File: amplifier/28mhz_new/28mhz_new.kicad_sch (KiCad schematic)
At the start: 32 parts, among them M1 RD16HHF1, Q1 LG, Q2 L6, Q3 LG, Q4 LG, Q5 LG

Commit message: Assigned all footprints
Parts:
- added RE3: 330, Resistor_SMD:R_1206_3216Metric_Pad1.30x1.75mm_HandSolder, symbol ltspice:res
- C1, C10, C14, C2, C6, C8, C9: footprint (none) -> Capacitor_SMD:C_0805_2012Metric_Pad1.18x1.45mm_HandSolder
- L1: footprint (none) -> B82144A2103K:INDAD3280W80L1200D520
- L2: footprint (none) -> 2929SQ-331GEC:2929SQ331GEC
- L5: footprint (none) -> 2222SQ:2222SQ181JEC
- L6, L7: footprint (none) -> 2929SQ-391GEC:2929SQ391GEC
- L8: value 440n -> 430n; footprint (none) -> 2929SQ-431GEC:2929SQ431GEC
- M1: footprint (none) -> Package_TO_SOT_THT:TO-220-3_Vertical
- Q1, Q3, Q4, Q5: value LG -> 2N3904; footprint (none) -> Package_TO_SOT_THT:TO-92L_HandSolder
- Q2: value L6 -> 2N3906; footprint (none) -> Package_TO_SOT_THT:TO-92L_HandSolder
- R1, R18, R9: footprint (none) -> Resistor_SMD:R_1206_3216Metric_Pad1.30x1.75mm_HandSolder
- R10, R11, R12, R13, R17, R20, R4, R8: footprint (none) -> Resistor_SMD:R_0603_1608Metric_Pad0.98x0.95mm_HandSolder
- R3: value 3.4k -> 3.3k; footprint (none) -> Resistor_SMD:R_0603_1608Metric_Pad0.98x0.95mm_HandSolder
- R7: value 165 -> 330; footprint (none) -> Resistor_SMD:R_1206_3216Metric_Pad1.30x1.75mm_HandSolder
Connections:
- net 0: now also M1.2 (S), RE3.2; no longer M1.3 (S)
- net VCC: now also R18.1
- net at C1.1, C2.2, L1.2: now also M1.3 (D); no longer M1.1 (D)
- net at Q2.3 (E), Q3.3 (E): now also M1.1 (G); no longer M1.2 (G)
- net at Q1.3 (E), R12.2, R13.1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: now also RE3.1
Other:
- note added: "IDEA: make this an RPi hat! If a user doesn't want to use it as a hat, then just solder directly to pins"
- moved on the sheet: R18, R7

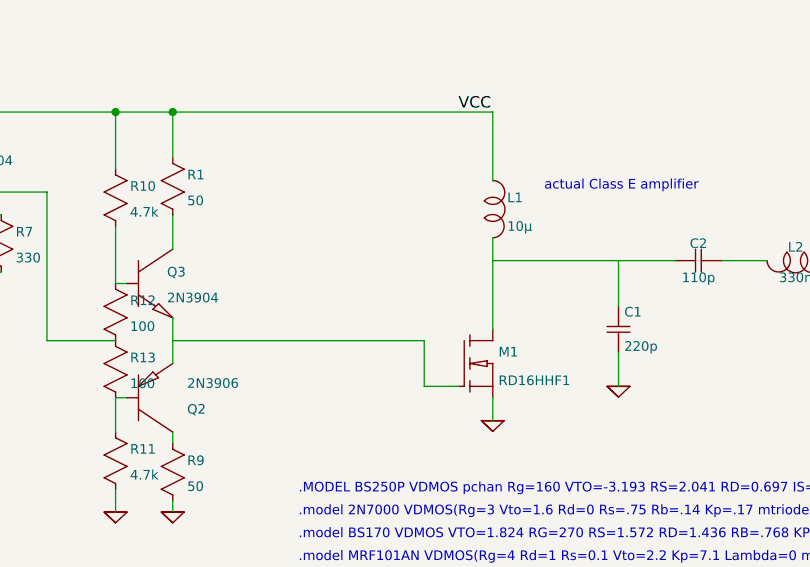
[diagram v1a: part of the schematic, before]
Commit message: This looks nice, but I'm realizing soldering it will be basically impossible
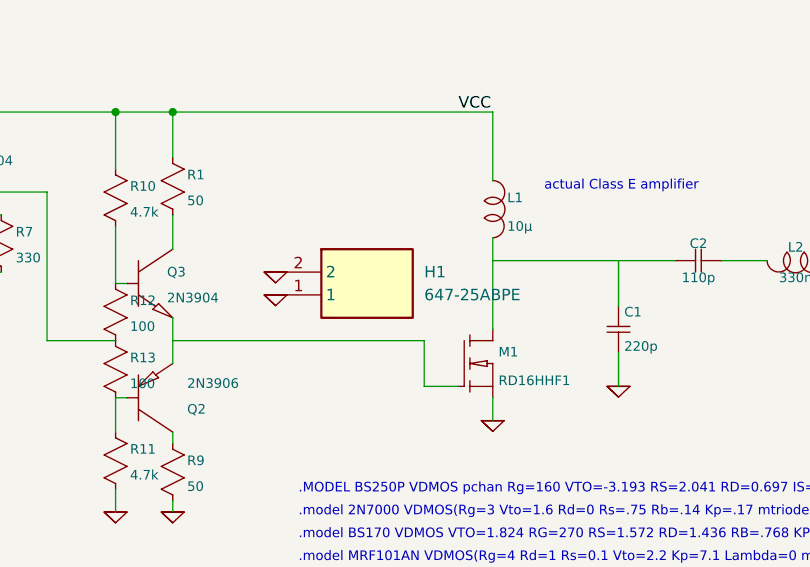
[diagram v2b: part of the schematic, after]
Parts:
- added H1: 647-25ABPE, 64725ABPE, symbol heatsink:647-25ABPE
- Q1, Q2, Q3, Q4, Q5: footprint Package_TO_SOT_THT:TO-92L_HandSolder -> Package_TO_SOT_THT:TO-92L_Inline
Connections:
- net 0: now also H1.1, H1.2

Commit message: NO DRC ERRORS
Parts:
- R10, R11, R12, R13, R20, R3, R4, R8: footprint Resistor_SMD:R_0603_1608Metric_Pad0.98x0.95mm_HandSolder -> Resistor_SMD:R_0805_2012Metric_Pad1.20x1.40mm_HandSolder
- R17: footprint Resistor_SMD:R_0603_1608Metric_Pad0.98x0.95mm_HandSolder -> Resistor_SMD:R_1206_3216Metric_Pad1.30x1.75mm_HandSolder
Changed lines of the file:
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@@
 			)
 		)
-		(property "Footprint" "Resistor_SMD:R_0603_1608Metric_Pad0.98x0.95mm_HandSolder"
+		(property "Footprint" "Resistor_SMD:R_0805_2012Metric_Pad1.20x1.40mm_HandSolder"
 			(at 86.36 102.87 0)
 			(effects
@@
 			)
 		)
-		(property "Description" "RT0603FRE071KL "
+		(property "Description" "RT0805FRE071KL "
 			(at 86.36 102.87 0)
 			(effects
@@
 			)
 		)
-		(property "Footprint" "Resistor_SMD:R_0603_1608Metric_Pad0.98x0.95mm_HandSolder"
+		(property "Footprint" "Resistor_SMD:R_0805_2012Metric_Pad1.20x1.40mm_HandSolder"
 			(at 93.98 107.95 0)
 			(effects
@@
 			)
 		)
-		(property "Description" "RT0603FRE0733RL"
+		(property "Description" "RT0805FRE0733RL"
 			(at 93.98 107.95 0)
 			(effects
@@
 			)
 		)
-		(property "Footprint" "Resistor_SMD:R_0603_1608Metric_Pad0.98x0.95mm_HandSolder"
+		(property "Footprint" "Resistor_SMD:R_0805_2012Metric_Pad1.20x1.40mm_HandSolder"
 			(at 121.92 82.55 0)
 			(effects
@@
 			)
 		)
-		(property "Description" "RT0603FRE074K7L"
+		(property "Description" "RT0805FRE074K7L"
 			(at 121.92 82.55 0)
 			(effects
@@
 			)
 		)
-		(property "Footprint" "Resistor_SMD:R_0603_1608Metric_Pad0.98x0.95mm_HandSolder"
+		(property "Footprint" "Resistor_SMD:R_0805_2012Metric_Pad1.20x1.40mm_HandSolder"
 			(at 121.92 101.6 0)
 			(effects
@@
 			)
 		)
-		(property "Description" "RT0603FRE07100RL"
+		(property "Description" "RT0805FRE07100RL"
 			(at 121.92 101.6 0)
 			(effects
@@
 			)
 		)
-		(property "Footprint" "Resistor_SMD:R_0603_1608Metric_Pad0.98x0.95mm_HandSolder"
+		(property "Footprint" "Resistor_SMD:R_1206_3216Metric_Pad1.30x1.75mm_HandSolder"
 			(at 68.58 102.87 0)
 			(effects
@@
 			)
 		)
-		(property "Description" "RT0603DRD07330RL"
+		(property "Description" "TNPW1206330RBEEA"
 			(at 68.58 102.87 0)
 			(effects
@@
 			)
 		)
-		(property "Footprint" "Resistor_SMD:R_0603_1608Metric_Pad0.98x0.95mm_HandSolder"
+		(property "Footprint" "Resistor_SMD:R_0805_2012Metric_Pad1.20x1.40mm_HandSolder"
 			(at 87.63 83.82 0)
 			(effects
@@
 			)
 		)
-		(property "Description" "RT0603FRE0710KL "
+		(property "Description" "RT0805FRE0710KL "
 			(at 87.63 83.82 0)
 			(effects
@@
 			)
 		)
-		(property "Footprint" "Resistor_SMD:R_0603_1608Metric_Pad0.98x0.95mm_HandSolder"
+		(property "Footprint" "Resistor_SMD:R_0805_2012Metric_Pad1.20x1.40mm_HandSolder"
 			(at 87.63 90.17 0)
 			(effects
@@
 			)
 		)
-		(property "Description" "RT0603FRD073K3L "
+		(property "Description" "RT0805FRD073K3L "
 			(at 87.63 90.17 0)
 			(effects
@@
 			)
 		)
-		(property "Footprint" "Resistor_SMD:R_0603_1608Metric_Pad0.98x0.95mm_HandSolder"
+		(property "Footprint" "Resistor_SMD:R_0805_2012Metric_Pad1.20x1.40mm_HandSolder"
 			(at 121.92 111.76 0)
 			(effects
@@
 			)
 		)
-		(property "Description" "RT0603FRE074K7L"
+		(property "Description" "RT0805FRE074K7L"
 			(at 121.92 111.76 0)
 			(effects
@@
 			)
 		)
-		(property "Footprint" "Resistor_SMD:R_0603_1608Metric_Pad0.98x0.95mm_HandSolder"
+		(property "Footprint" "Resistor_SMD:R_0805_2012Metric_Pad1.20x1.40mm_HandSolder"
 			(at 121.92 95.25 0)
 			(effects
@@
 			)
 		)
-		(property "Description" "RT0603FRE07100RL"
+		(property "Description" "RT0805FRE07100RL"
 			(at 121.92 95.25 0)
 			(effects

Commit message: SEND IT (in the morning once i have sanity checked)
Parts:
- added B1: CONBNC002, BNC:CONBNC002, symbol BNC:CONBNC002
- added J1: GPIO, Connector_PinSocket_2.54mm:PinSocket_2x20_P2.54mm_Vertical, symbol Connector_Generic:Conn_02x20_Odd_Even
- added J2: 694106301002, barreljack:694106301002_1, symbol barreljack:694106301002
- H1: footprint 64725ABPE -> heatsink:64725ABPE
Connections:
- net 0: now also B1.1, J1.14 (Pin_14), J1.20 (Pin_20), J1.25 (Pin_25), J1.30 (Pin_30), J1.34 (Pin_34), J1.39 (Pin_39), J1.6 (Pin_6), J1.9 (Pin_9), J2.2 (GND_1), J2.3 (GND_2)
- net RF_OUT: now also B1.2
- net VCC: now also J2.1 (POWER)
- net RF_IN renamed GPIO4/GPCLK0
- new net +3V3: J1.1 (Pin_1), J1.17 (Pin_17)
- new net +5V: J1.2 (Pin_2), J1.4 (Pin_4)
- new net GPIO10/SPI0.MOSI: J1.19 (Pin_19)
- new net GPIO11/SPI0.SCLK: J1.23 (Pin_23)
- new net GPIO12/PWM0: J1.32 (Pin_32)
- new net GPIO13/PWM1: J1.33 (Pin_33)
- new net GPIO14/TXD0: J1.8 (Pin_8)
- new net GPIO15/RXD0: J1.10 (Pin_10)
- new net GPIO16: J1.36 (Pin_36)
- new net GPIO17: J1.11 (Pin_11)
- new net GPIO18/PCM.CLK: J1.12 (Pin_12)
- new net GPIO19/PCM.FS: J1.35 (Pin_35)
- new net GPIO20/PCM.DIN: J1.38 (Pin_38)
- new net GPIO21/PCM.DOUT: J1.40 (Pin_40)
- new net GPIO22: J1.15 (Pin_15)
- new net GPIO23: J1.16 (Pin_16)
- new net GPIO24: J1.18 (Pin_18)
- new net GPIO25: J1.22 (Pin_22)
- new net GPIO26: J1.37 (Pin_37)
- new net GPIO27: J1.13 (Pin_13)
- new net GPIO2/SDA1: J1.3 (Pin_3)
- new net GPIO3/SCL1: J1.5 (Pin_5)
- new net GPIO4/GPCLK0: J1.7 (Pin_7)
- new net GPIO5: J1.29 (Pin_29)
- new net GPIO6: J1.31 (Pin_31)
- new net GPIO7/SPI0.CE1: J1.26 (Pin_26)
- new net GPIO8/SPI0.CE0: J1.24 (Pin_24)
- new net GPIO9/SPI0.MISO: J1.21 (Pin_21)
- new net ID_SCL: J1.28 (Pin_28)
- new net ID_SDA: J1.27 (Pin_27)
- no-connect marks 0 -> 2
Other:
- moved on the sheet: C1, C10, C14, C2, C6, C8, C9, H1, L1, L2, L5, L6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

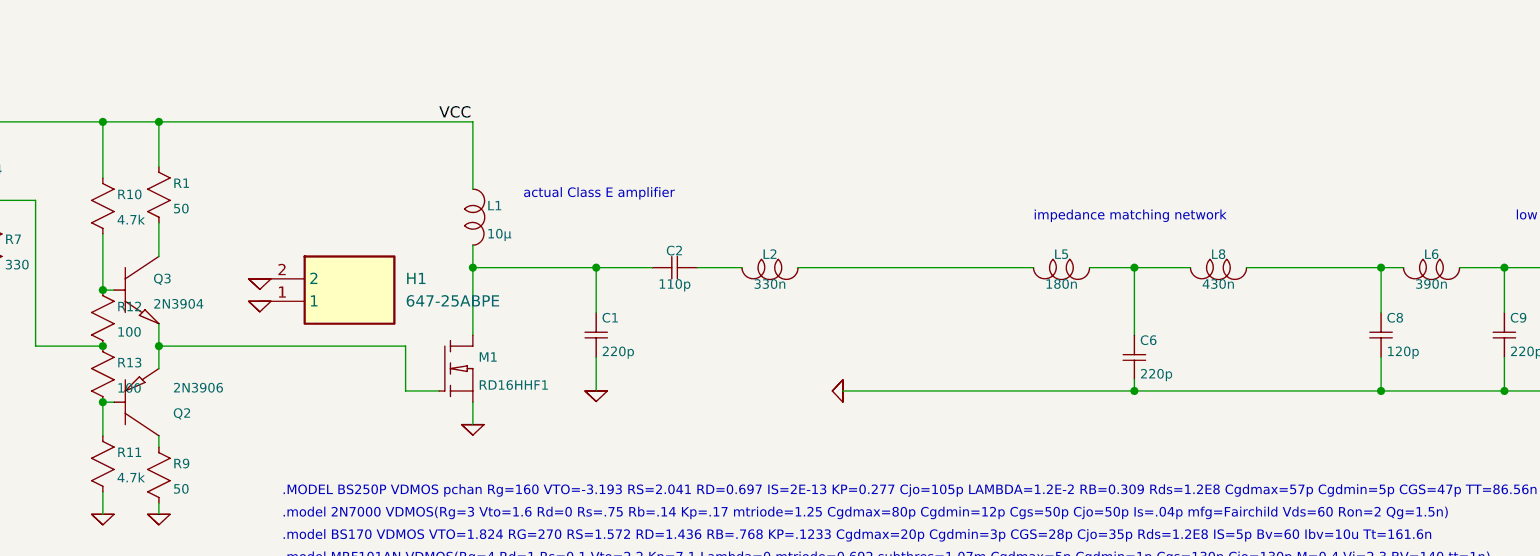
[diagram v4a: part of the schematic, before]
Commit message: Add zero ohm resistors
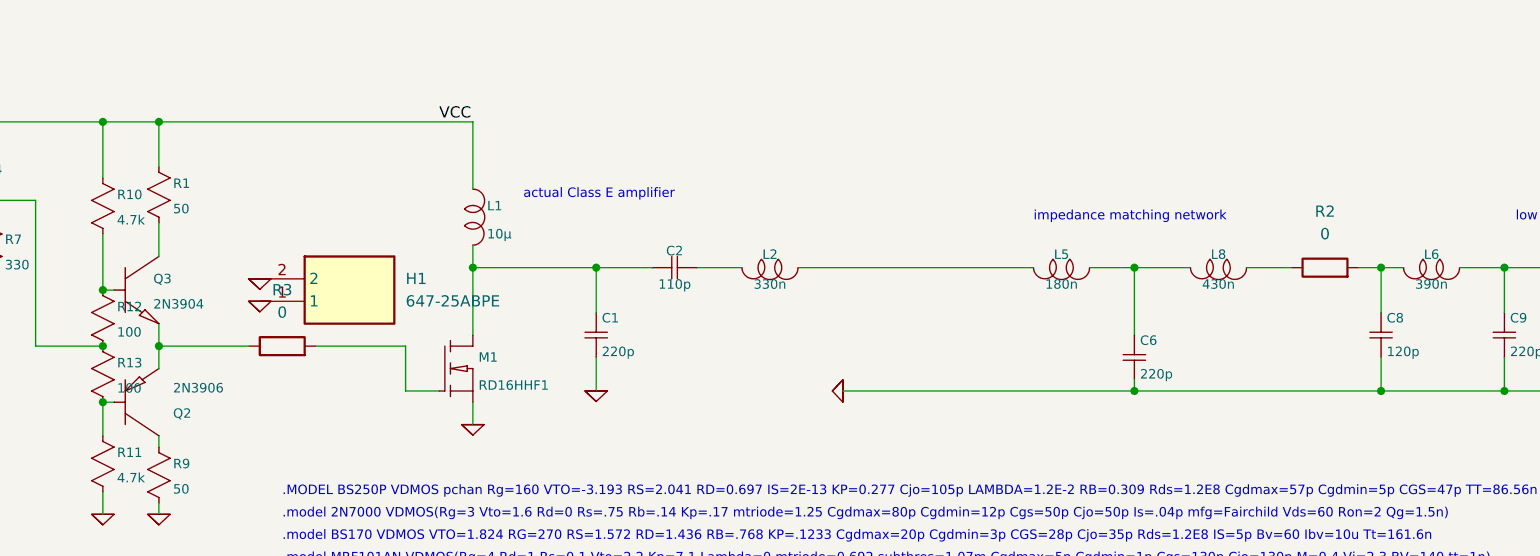
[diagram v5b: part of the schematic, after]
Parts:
- added R2, R3: 0, Resistor_SMD:R_2512_6332Metric, symbol Device:R
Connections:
- net at Q2.3 (E), Q3.3 (E): now also R3.1; no longer M1.1 (G)
- net at C8.1, L6.2: now also R2.2; no longer L8.1
- new net: L8.1, R2.1
- new net: M1.1 (G), R3.2
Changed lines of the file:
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@@
 	(wire
 		(pts
+			(xy 222.25 93.98) (xy 217.17 93.98)
+		)
+		(stroke
+			(width 0.1524)
+			(type solid)
+		)
+	)
+	(wire
+		(pts
 			(xy 262.89 93.98) (xy 269.24 93.98)
 		)
@@
 	(wire
 		(pts
-			(xy 232.41 93.98) (xy 217.17 93.98)
+			(xy 104.14 102.87) (xy 93.98 102.87)
+		)
+		(stroke
+			(width 0.1524)
+			(type solid)
+		)
+	)
+	(wire
+		(pts
+			(xy 232.41 93.98) (xy 229.87 93.98)
 		)
 		(stroke
@@
 	(wire
 		(pts
-			(xy 121.92 102.87) (xy 93.98 102.87)
+			(xy 121.92 102.87) (xy 111.76 102.87)
 		)
 		(stroke
@@
 	)
 	(symbol
+		(lib_id "Device:R")
+		(at 107.95 102.87 90)
+		(unit 1)
+		(exclude_from_sim no)
+		(in_bom yes)
+		(on_board yes)
+		(dnp no)
+		(fields_autoplaced yes)
+		(property "Reference" "R3"
+			(at 107.95 96.52 90)
+			(effects
+				(font
+					(size 1.27 1.27)
+				)
+			)
+		)
+		(property "Value" "0"
+			(at 107.95 99.06 90)
+			(effects
+				(font
+					(size 1.27 1.27)
+				)
+			)
+		)
+		(property "Footprint" "Resistor_SMD:R_2512_6332Metric"
+			(at 107.95 104.648 90)
+			(effects
+				(font
+					(size 1.27 1.27)
+				)
+				(hide yes)
+			)
+		)
+		(property "Datasheet" "~"
+			(at 107.95 102.87 0)
+			(effects
+				(font
+					(size 1.27 1.27)
+				)
+				(hide yes)
+			)
+		)
+		(property "Description" "Resistor"
+			(at 107.95 102.87 0)
+			(effects
+				(font
+					(size 1.27 1.27)
+				)
+				(hide yes)
+			)
+		)
+		(pin "2"
+		)
+		(pin "1"
+		)
+		(instances
+			(project "28mhz_new"
+				(path "/a27f0a38-2c6c-4fbf-aebb-5f1ef9203ab8"
+					(reference "R3")
+					(unit 1)
+				)
+			)
+		)
+	)
+	(symbol
 		(lib_id "ltspice:res")
 		(at 86.36 101.6 0)
@@
 					(unit 1)
 				)
+			)
+		)
+	)
+	(symbol
+		(lib_id "Device:R")
+		(at 226.06 93.98 90)
+		(unit 1)
+		(exclude_from_sim no)
+		(in_bom yes)
+		(on_board yes)
+		(dnp no)
+		(fields_autoplaced yes)
+		(property "Reference" "R2"
+			(at 226.06 87.63 90)
+			(effects
+				(font
+					(size 1.27 1.27)
+				)
+			)
+		)
+		(property "Value" "0"
+			(at 226.06 90.17 90)
+			(effects
+				(font
+					(size 1.27 1.27)
+				)
+			)
+		)
+		(property "Footprint" "Resistor_SMD:R_2512_6332Metric"
+			(at 226.06 95.758 90)
+			(effects
+				(font
+					(size 1.27 1.27)
+				)
+				(hide yes)
+			)
+		)
+		(property "Datasheet" "~"
+			(at 226.06 93.98 0)
+			(effects
+				(font
+					(size 1.27 1.27)
+				)
+				(hide yes)
+			)
+		)
+		(property "Description" "Resistor"
+			(at 226.06 93.98 0)
+			(effects
+				(font
+					(size 1.27 1.27)
+				)
+				(hide yes)
+			)
+		)
+		(pin "2"
+		)
+		(pin "1"
+		)
+		(instances
+			(project "28mhz_new"
+				(path "/a27f0a38-2c6c-4fbf-aebb-5f1ef9203ab8"
+					(reference "R2")
+					(unit 1)
+				)

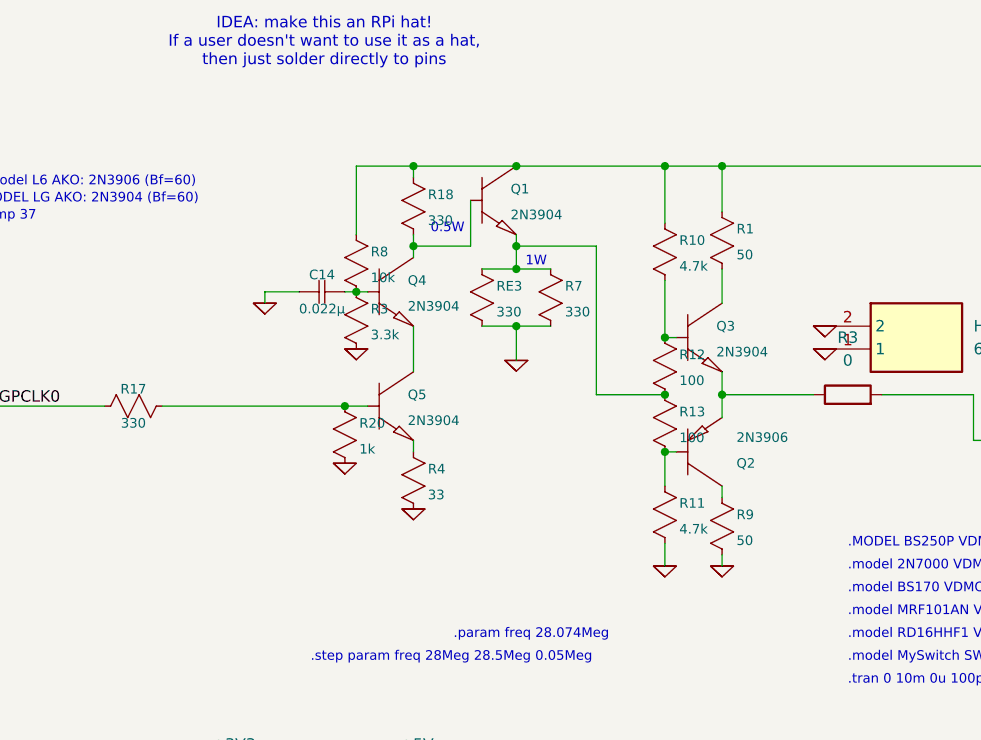
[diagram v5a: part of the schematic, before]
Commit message: Fix 3904 and 3906 transistor pinout
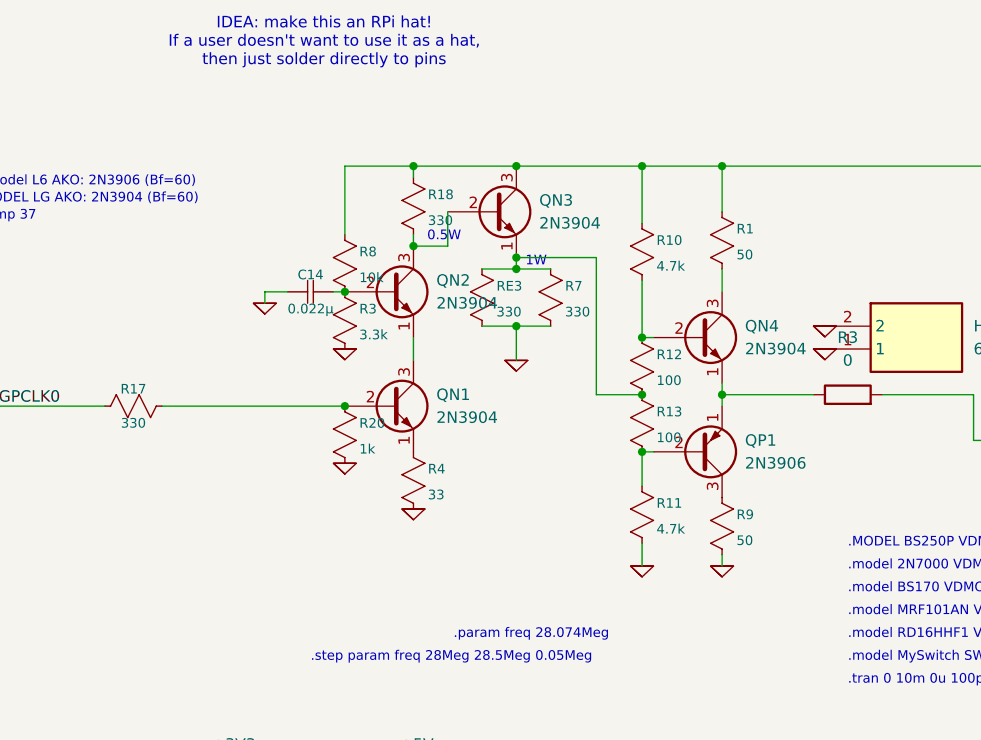
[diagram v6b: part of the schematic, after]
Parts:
- removed Q1, Q3, Q4, Q5: 2N3904, Package_TO_SOT_THT:TO-92L_Inline, symbol ltspice:npn
- removed Q2: 2N3906, Package_TO_SOT_THT:TO-92L_Inline, symbol ltspice:pnp
- added QN1, QN2, QN3, QN4: 2N3904, Package_TO_SOT_THT:TO-92L_Inline, symbol Device:Q_NPN_EBC
- added QP1: 2N3906, Package_TO_SOT_THT:TO-92L_Inline, symbol Device:Q_PNP_EBC
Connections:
- net VCC: now also QN3.3 (C)
- net at R1.2: now also QN4.3 (C)
- net at R10.2, R12.1: now also QN4.2 (B)
- net at R3.1: now also QN4.1 (E), QP1.1 (E)
- net at R18.2: now also QN2.3 (C), QN3.2 (B)
- net at R17.1, R20.1: now also QN1.2 (B)
- net at R12.2, R13.1, R7.1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: now also QN3.1 (E)
- net at R4.1: now also QN1.1 (E)
- net at R9.1: now also QP1.3 (C)
- net at R11.1, R13.2: now also QP1.2 (B)
- net at C14.1, R3.1, R8.2: now also QN2.2 (B)
- new net: QN1.3 (C), QN2.1 (E)
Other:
- moved on the sheet: C14, R10, R11, R12, R13, R3, R8
